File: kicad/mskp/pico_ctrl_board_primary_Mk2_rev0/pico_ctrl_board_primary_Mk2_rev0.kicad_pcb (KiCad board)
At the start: 2 copper layers, 24 parts, among them J1 USB_C_I2C_Receptacle, J2 SPI-JST, J3 RJ45_I2C_SPI_Port, J4 UART-JST, J5 I2C-aux-pad, J6 OLED_128x64, J7 Keypad-Matrix_JST, J8 USB-sw-ctrl, J9 Debug_pads, SW1 RESET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

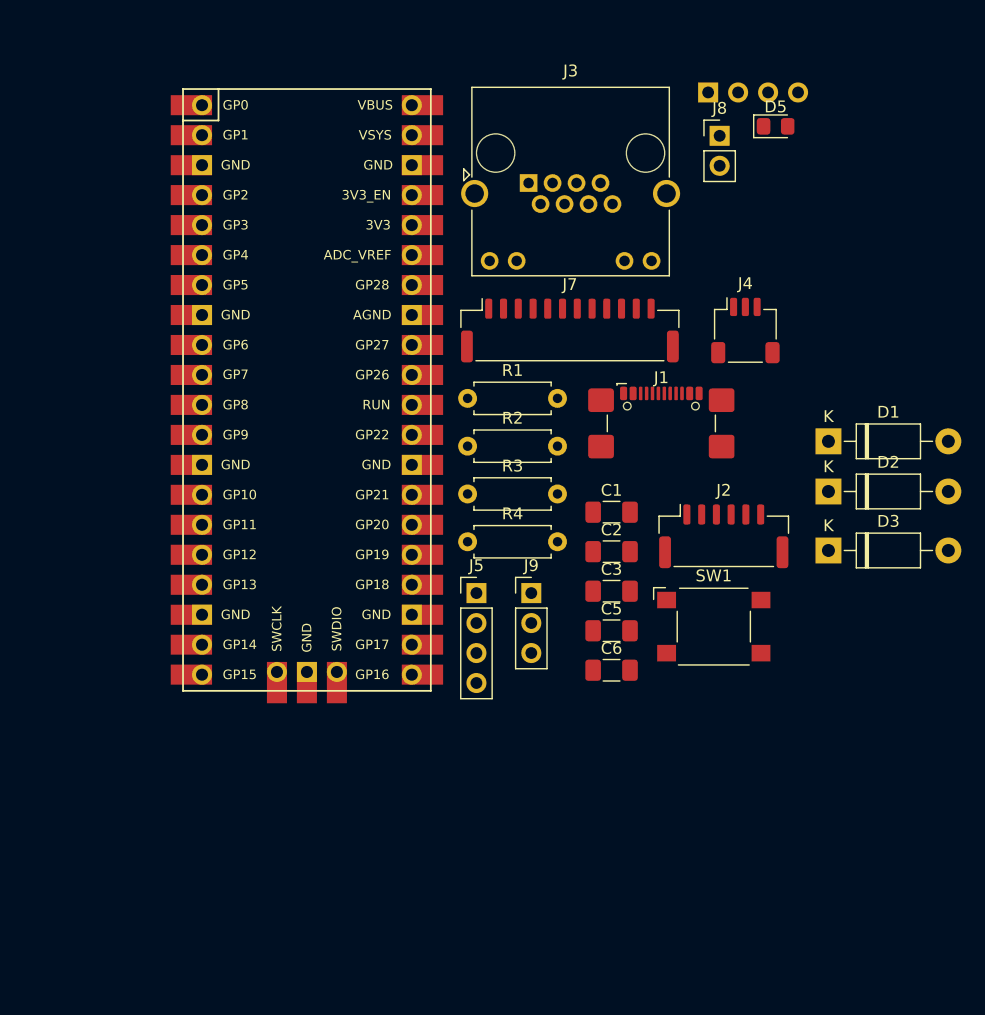
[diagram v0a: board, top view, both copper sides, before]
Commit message: Begins rough PCB part grouping for all control board revisions
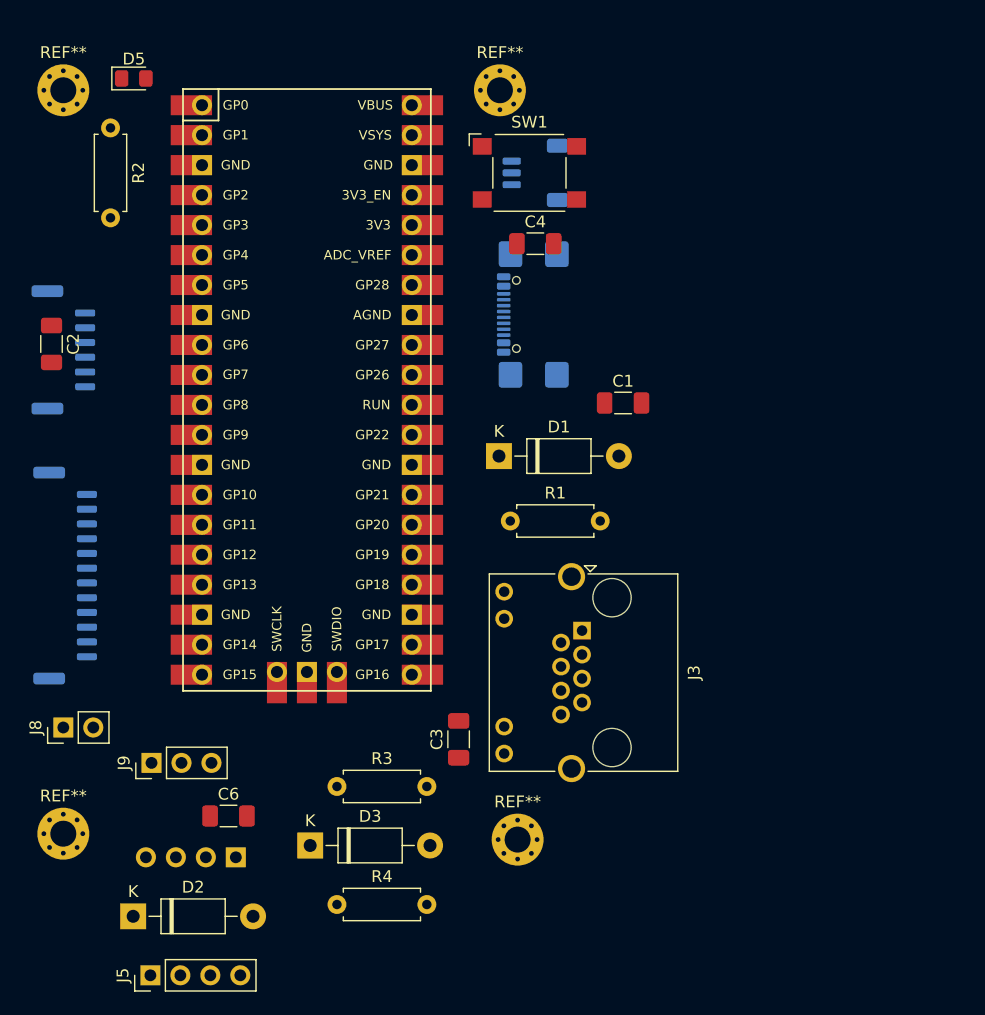
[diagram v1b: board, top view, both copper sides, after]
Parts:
- removed C5: 100uF, Capacitor_SMD:C_1206_3216Metric_Pad1.33x1.80mm_HandSolder
- added C4: 100uF, Capacitor_SMD:C_1206_3216Metric_Pad1.33x1.80mm_HandSolder, F.Cu at (149.0, 62.0)
- added REF**: MountingHole_2.2mm_M2_Pad_Via, MountingHole:MountingHole_2.2mm_M2_Pad_Via, F.Cu at (109.0, 112.0)
- added REF**: MountingHole_2.2mm_M2_Pad_Via, MountingHole:MountingHole_2.2mm_M2_Pad_Via, F.Cu at (147.5, 112.5)
- added REF**: MountingHole_2.2mm_M2_Pad_Via, MountingHole:MountingHole_2.2mm_M2_Pad_Via, F.Cu at (109.0, 49.0)
- added REF**: MountingHole_2.2mm_M2_Pad_Via, MountingHole:MountingHole_2.2mm_M2_Pad_Via, F.Cu at (146.0, 49.0)
- J1, J2, J4, J7: moved to B.Cu
- moved J6 80.4 mm to (119.8, 114.0), turned to 180 degrees
- moved J8 74.9 mm to (109.0, 103.0), turned to 90 degrees
- moved D2 69.0 mm to (114.9, 119.0)
- moved J2 58.2 mm to (109.0, 71.0), turned to 90 degrees
- moved D5 54.5 mm to (115.0, 48.0)
- moved C2 50.6 mm to (108.0, 70.5), turned to -90 degrees
- moved D3 50.5 mm to (129.9, 113.0)
- moved J7 47.6 mm to (109.2, 90.1), turned to 90 degrees
- moved J5 42.6 mm to (116.4, 124.0), turned to 90 degrees
- moved SW1 41.5 mm to (148.5, 56.0)
- moved R2 40.5 mm to (113.0, 52.2), turned to -90 degrees
- moved J3 38.2 mm to (153.0, 94.8), turned to -90 degrees
- moved J9 35.3 mm to (116.5, 106.0), turned to 90 degrees
- moved C6 34.7 mm to (123.0, 110.5)
- moved R4 32.7 mm to (132.2, 118.0)
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
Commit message: Continues work with rough PCB outlines
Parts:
- moved R2 42.5 mm to (155.5, 54.2)
- moved D5 37.1 mm to (151.5, 54.8), turned to 90 degrees
- moved D3 24.8 mm to (144.9, 93.2)
- moved R1 23.9 mm to (144.2, 61.8)
- moved J1 16.0 mm to (154.5, 83.4)
- moved J5 14.2 mm to (124.3, 112.2), turned to -90 degrees
- moved J6 14.1 mm to (128.9, 103.2)
- moved J4 13.9 mm to (155.0, 68.5)
- moved C3 13.6 mm to (129.5, 108.0), turned to -90 degrees
- moved J7 12.3 mm to (110.7, 77.9)
- moved J8 12.3 mm to (110.0, 90.7), turned to 0 degrees
- moved SW1 12.3 mm to (148.2, 68.2)
- moved D2 11.8 mm to (115.4, 107.2)
- moved C2 11.0 mm to (109.7, 59.6)
- moved J2 11.0 mm to (110.7, 60.1)
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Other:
- board outline added: 50.5 x 72 mm

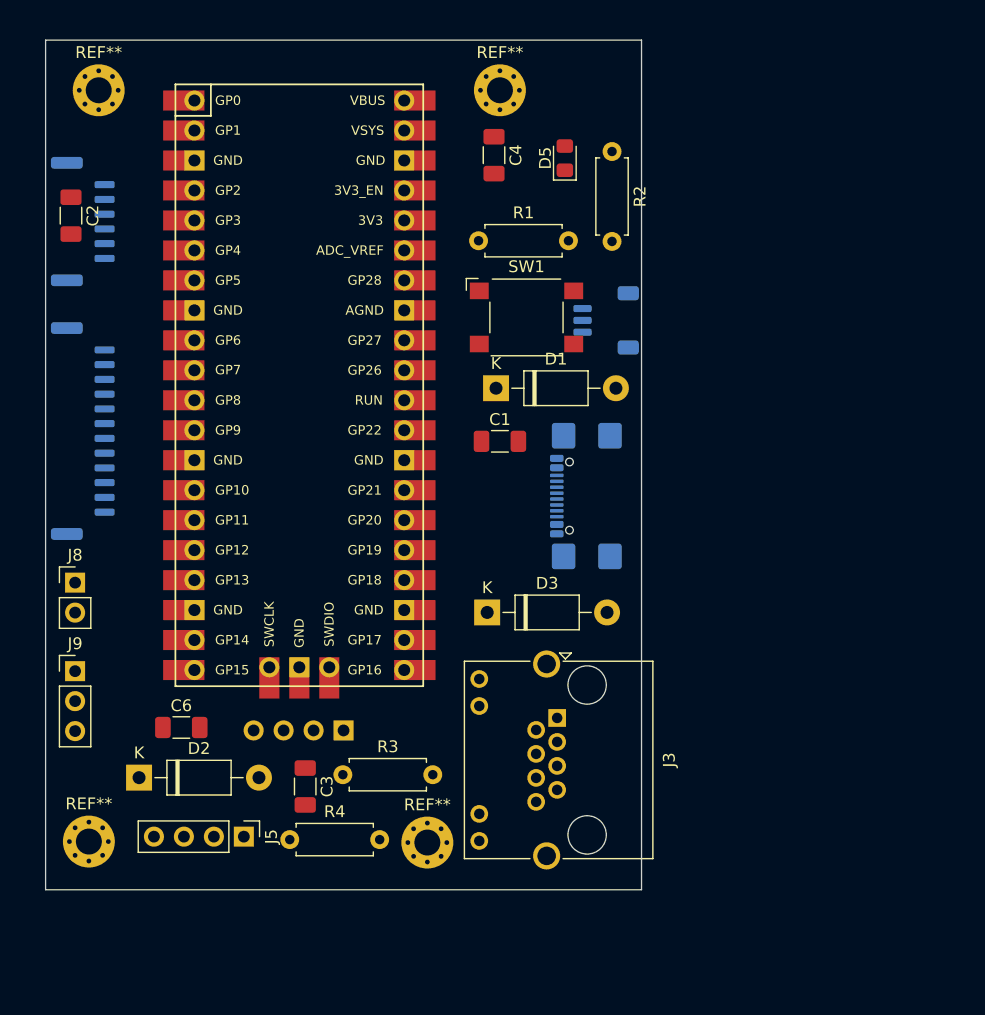
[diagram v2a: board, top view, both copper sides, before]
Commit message: Refining PCB outlines for pico and io control boards
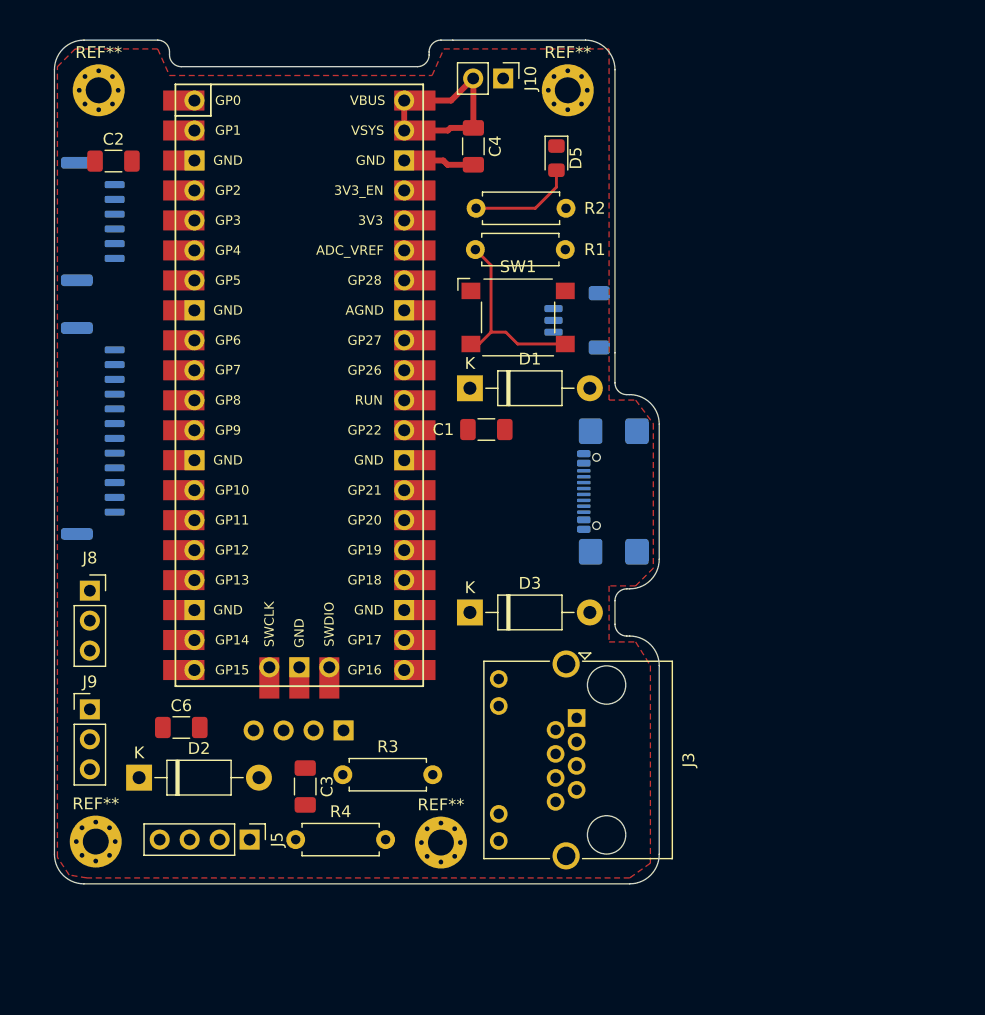
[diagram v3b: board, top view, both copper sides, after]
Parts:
- added J10: Conn_01x02_Socket, Connector_PinHeader_2.54mm:PinHeader_1x02_P2.54mm_Vertical, F.Cu at (146.3, 48.0)
- J8: value USB-sw-ctrl -> USB_sw_ctrl; footprint Connector_PinHeader_2.54mm:PinHeader_1x02_P2.54mm_Vertical -> Connector_PinSocket_2.54mm:PinSocket_1x03_P2.54mm_Vertical
- moved R2 12.5 mm to (144.0, 59.0), turned to 0 degrees
- moved C2 5.86 mm to (113.2, 55.0), turned to 0 degrees
- moved REF** 5.75 mm to (151.8, 49.0)
- moved J9 3.47 mm to (111.2, 101.5)
- moved J4 2.46 mm to (152.5, 68.5)
- moved J1 2.32 mm to (156.8, 83.0)
- moved D1 2.21 mm to (143.5, 74.2)
- moved C4 1.90 mm to (143.8, 53.8)
- moved J3 1.65 mm to (152.5, 102.2)
- moved C1 1.52 mm to (144.9, 77.8), turned to 180 degrees
- moved D3 1.46 mm to (143.5, 93.2)
- moved J8 1.42 mm to (111.2, 91.4)
- moved REF** 1.15 mm to (141.0, 112.8)
- moved J2 0.85 mm to (111.5, 60.1)
- moved J7 0.85 mm to (111.5, 77.9)
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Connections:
- C1 pad 1: Net-(D1-K) -> +5V
- C6 pad 1: +5V -> Net-(J6-VCC)
- J6 pad 2: +5V -> Net-(J6-VCC)
- J8 pad 1: /SEL -> GND
- J8 pad 2: /SUS -> /SEL
- J9 pad 1: /SWDIO -> GND
- J9 pad 2: GND -> /SWDIO
- U1 pad 13: unconnected-(U1-GND-Pad13) -> GND
- U1 pad 18: unconnected-(U1-GND-Pad18) -> GND
- U1 pad 23: unconnected-(U1-GND-Pad23) -> GND
- U1 pad 28: unconnected-(U1-GND-Pad28) -> GND
- U1 pad 3: unconnected-(U1-GND-Pad3) -> GND
- U1 pad 36: unconnected-(U1-3V3-Pad36)_0 -> Net-(J6-VCC)
- U1 pad 42: GND -> unconnected-(U1-GND-Pad42)_0
- U1 pad 8: unconnected-(U1-GND-Pad8) -> GND
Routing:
- net +5V: track 0.00 -> 19.3 mm
- net Net-(R1-Pad1): track 0.00 -> 16.4 mm
- net Net-(D5-A): track 0.00 -> 8.99 mm
- net GND: track 0.00 -> 6.01 mm
- added copper zone on F.Cu, net GND
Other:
- board size 50.5 x 72 mm -> 51.2 x 71.5 mm

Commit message: Initial layout work on pico_ctrl_board_primary_Mk2_rev0 PCB
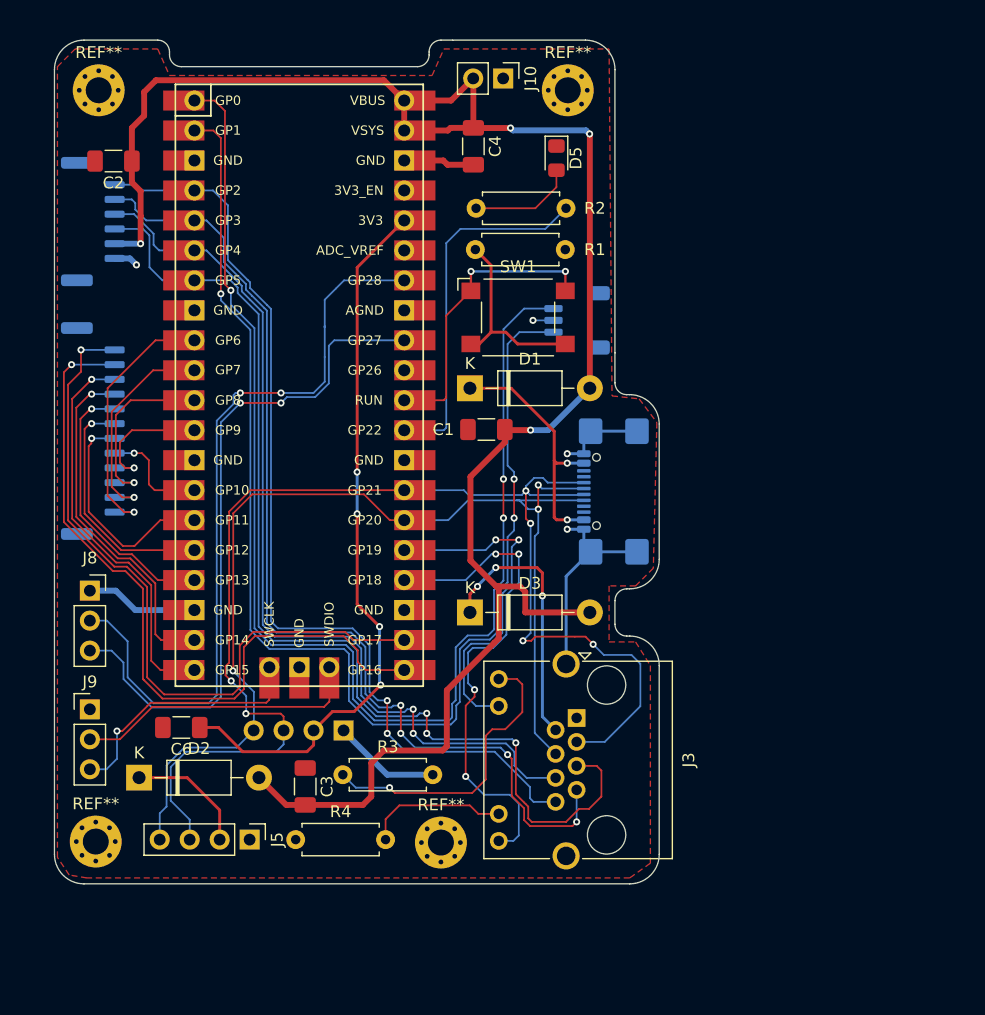
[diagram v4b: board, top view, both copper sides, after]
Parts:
- turned C2 to 180 degrees
- turned C6 to 180 degrees
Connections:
- J1 pad S1: unconnected-(J1-SHIELD-PadS1)_1 -> GND
- J3 pad SH: unconnected-(J3-PadSH)_0 -> GND
- U1 pad 42: unconnected-(U1-GND-Pad42)_0 -> GND
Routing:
- net +5V: track 19.3 -> 159.8 mm, vias 0 -> 4
- net /SCL: track 0.00 -> 112.3 mm, vias 0 -> 6
- net Net-(J4-Pin_1): track 0.00 -> 110.9 mm, vias 0 -> 3
- net Net-(J4-Pin_3): track 0.00 -> 107.9 mm, vias 0 -> 3
- net /SDA: track 0.00 -> 96.0 mm, vias 0 -> 3
- net /CSn: track 0.00 -> 91.5 mm, vias 0 -> 3
- net /TX: track 0.00 -> 87.6 mm, vias 0 -> 4
- net /SCK: track 0.00 -> 82.1 mm, vias 0 -> 2
- net /RX: track 0.00 -> 77.9 mm, vias 0 -> 2
- net /SEL: track 0.00 -> 64.5 mm, vias 0 -> 2
- net Net-(J7-Pin_11): track 0.00 -> 62.8 mm, vias 0 -> 1
- net Net-(J7-Pin_12): track 0.00 -> 61.4 mm, vias 0 -> 1
- net Net-(J6-VCC): track 0.00 -> 61.1 mm, vias 0 -> 4
- net /SUS: track 0.00 -> 57.8 mm, vias 0 -> 2
- net GND: track 6.01 -> 54.1 mm, vias 0 -> 4
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
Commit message: Adds silkscreen for pico_ctrl_board_primary_Mk2_rev0
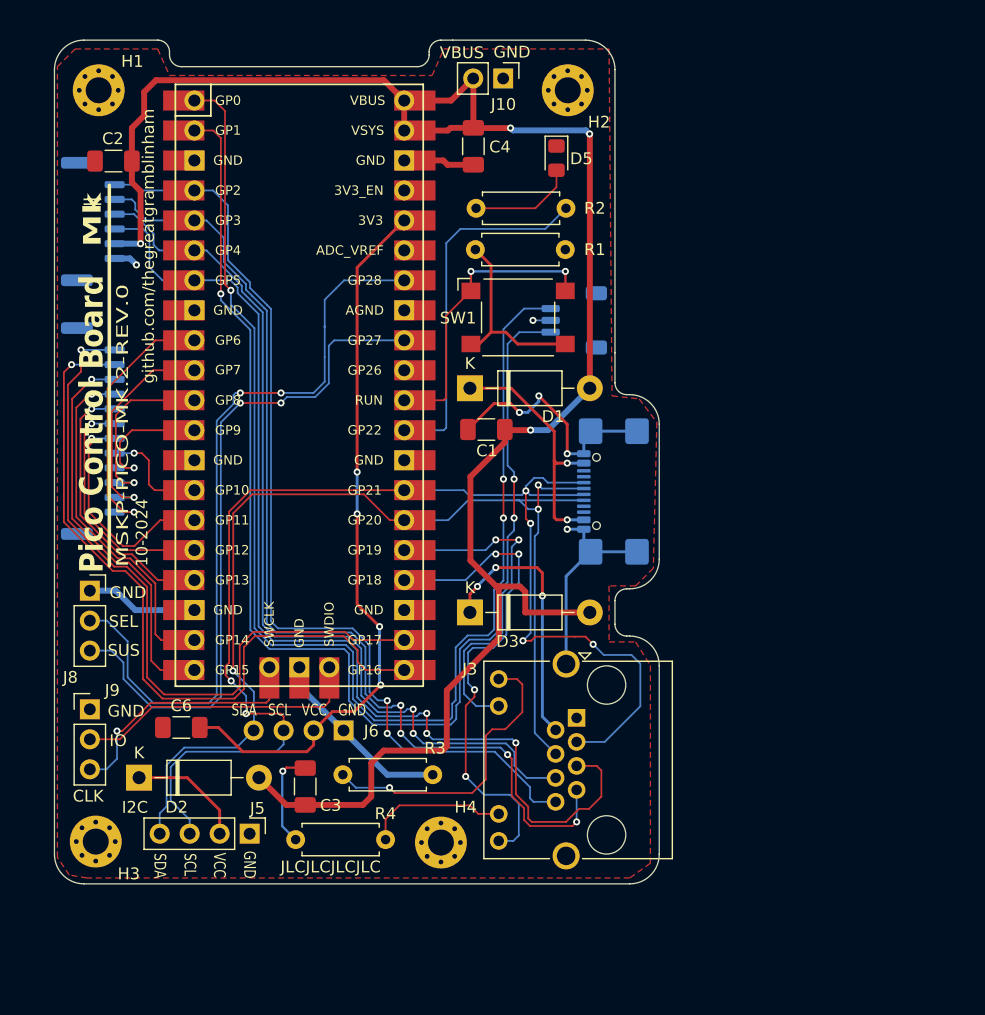
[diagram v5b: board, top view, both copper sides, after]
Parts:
- moved J5 0.50 mm to (124.8, 112.0)
- moved J4 0.24 mm to (152.3, 68.5)
- renumbered REF** to H1, REF** to H2, REF** to H3, REF** to H4
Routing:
- net GND: track 54.1 -> 83.3 mm, vias 4 -> 7
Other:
- board text added: "10-2024"
- board text added: "CLK"
- board text added: "CSn"
- board text added: "GND"
- board text added: "I2C"
- board text added: "I2C + SPI"
- board text added: "II"
- board text added: "IO"
- board text added: "JLCJLCJLCJLC"
- board text added: "KEYPAD MODULE"
- board text added: "MSKP-PICO-MK.2-REV.0"
- board text added: "Mk"
- board text added: "Pico Control Board"
- board text added: "RX"
- board text added: "SCK"
- board text added: "SCL"
- board text added: "SDA"
- board text added: "SEL"
- board text added: "SPI"
- board text added: "SUS"
- board text added: "TX"
- board text added: "UART"
- board text added: "VBUS"
- board text added: "VCC"
- board text added: "github.com/thegreatgramblinham"
